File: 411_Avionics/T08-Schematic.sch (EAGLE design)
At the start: 42 parts, among them IC1 BQ24022, J1 USB-MICROB, J3 JST-PH-2-SMT-RA, U1 LP5907, U2 M25P10-AVMN6TP_TR, U3 LSM9DS0, U5 LTC1998, U6 ATMEGA32U4-AU, X1 8MHz

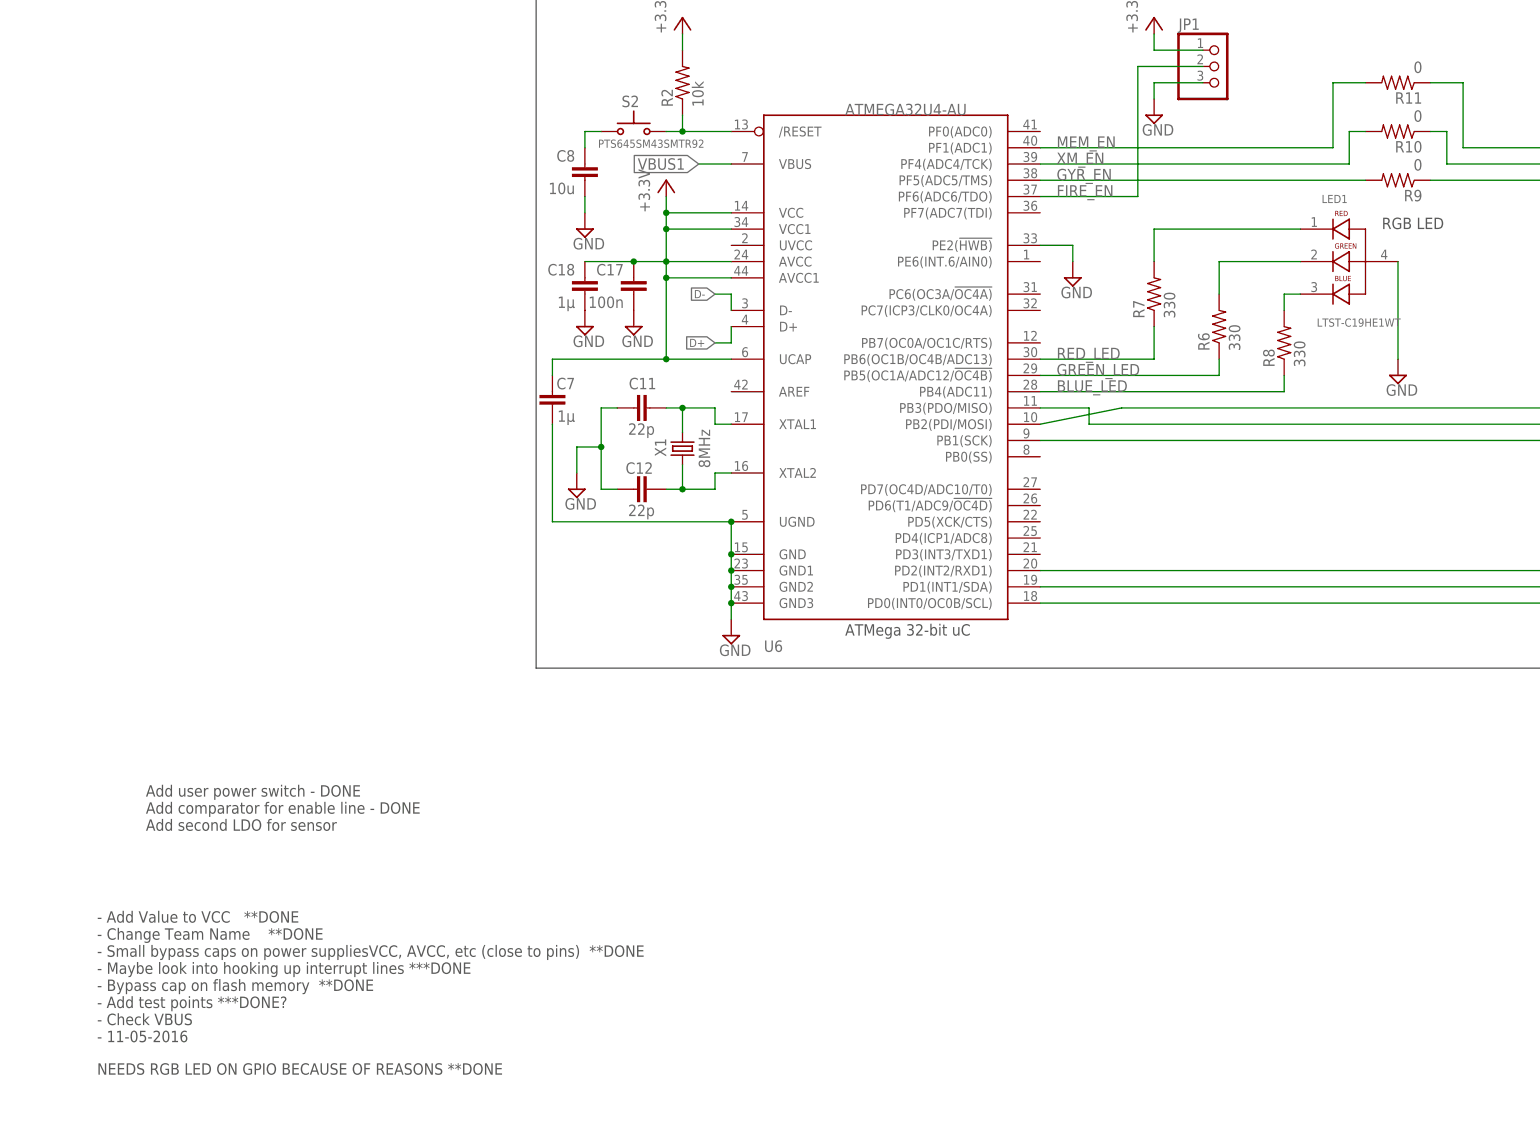
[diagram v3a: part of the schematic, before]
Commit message: Added resistors to D+/D-, removed incorrect reset button cap, fixed RGB LED VCC
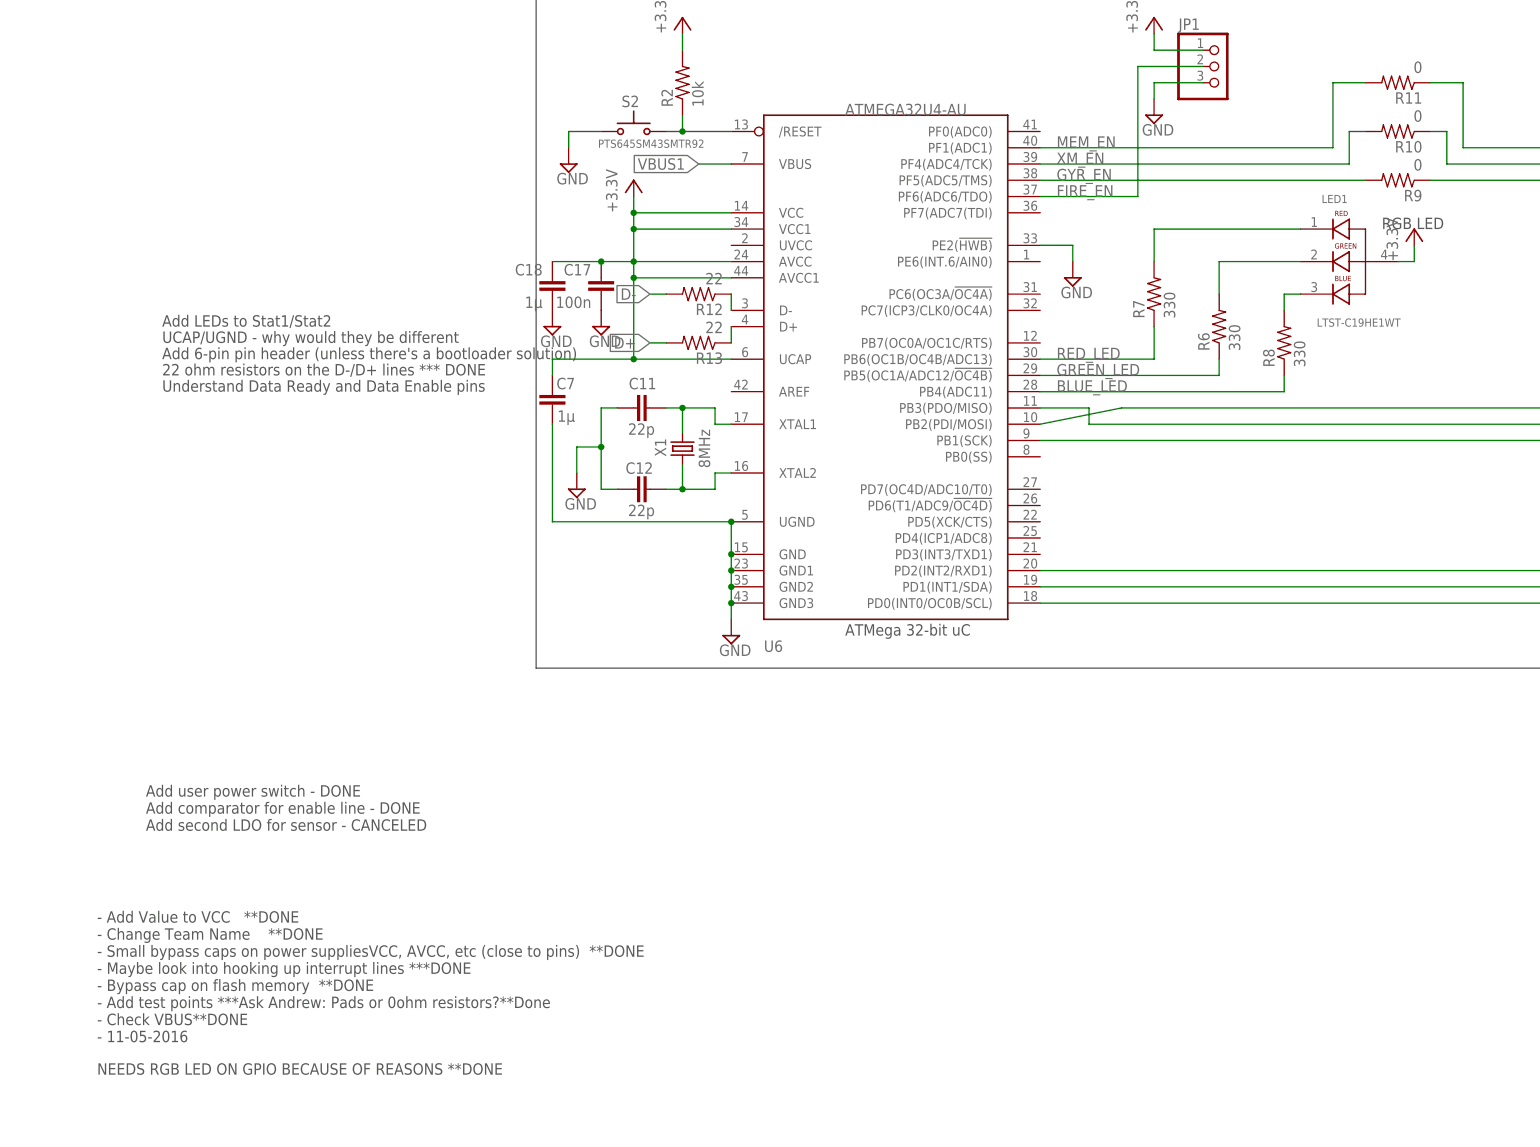
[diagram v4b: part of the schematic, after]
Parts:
- removed C8: 10u, rcl:C-EUC0603
- added R12, R13: 22, rcl:R-US_R0603
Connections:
- new net N$47: R13.1, U6.D+
- net D+: now also R13.2; no longer U6.D+
- net D-: now also R12.2; no longer U6.D-
- net GND: now also S2.P; no longer C8.2, LED1.4
- net N$6: now also R12.1, U6.D-; no longer C8.1, S2.P
- net VCC: now also LED1.4
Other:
- note added: "- Add Value to VCC **DONE - Change Team Name **DONE - Small bypass caps on power suppliesVCC, AVCC, etc (close to pins) **DONE - Maybe look into hooking up interrupt lines ***DONE - Bypass cap on flash memory **DONE - Add test points ***Ask Andrew: Pads or 0ohm resistors?**Done - Check VBUS**DONE - 11-05-2016"
- note added: "22 ohm resistors on the D-/D+ lines *** DONE"
- note added: "Add 6-pin pin header (unless there's a bootloader solution)"
- note added: "Add LEDs to Stat1/Stat2"
- note added: "Add user power switch - DONE Add comparator for enable line - DONE Add second LDO for sensor - CANCELED"
- note added: "UCAP/UGND - why would they be different"
- note added: "Understand Data Ready and Data Enable pins"
- note removed: "- Add Value to VCC **DONE - Change Team Name **DONE - Small bypass caps on power suppliesVCC, AVCC, etc (close to pins) **DONE - Maybe look into hooking up interrupt lines ***DONE - Bypass cap on flash memory **DONE - Add test points ***DONE? - Check VBUS - 11-05-2016"
- note removed: "Add user power switch - DONE Add comparator for enable line - DONE Add second LDO for sensor"
- moved on the sheet: C17, C18

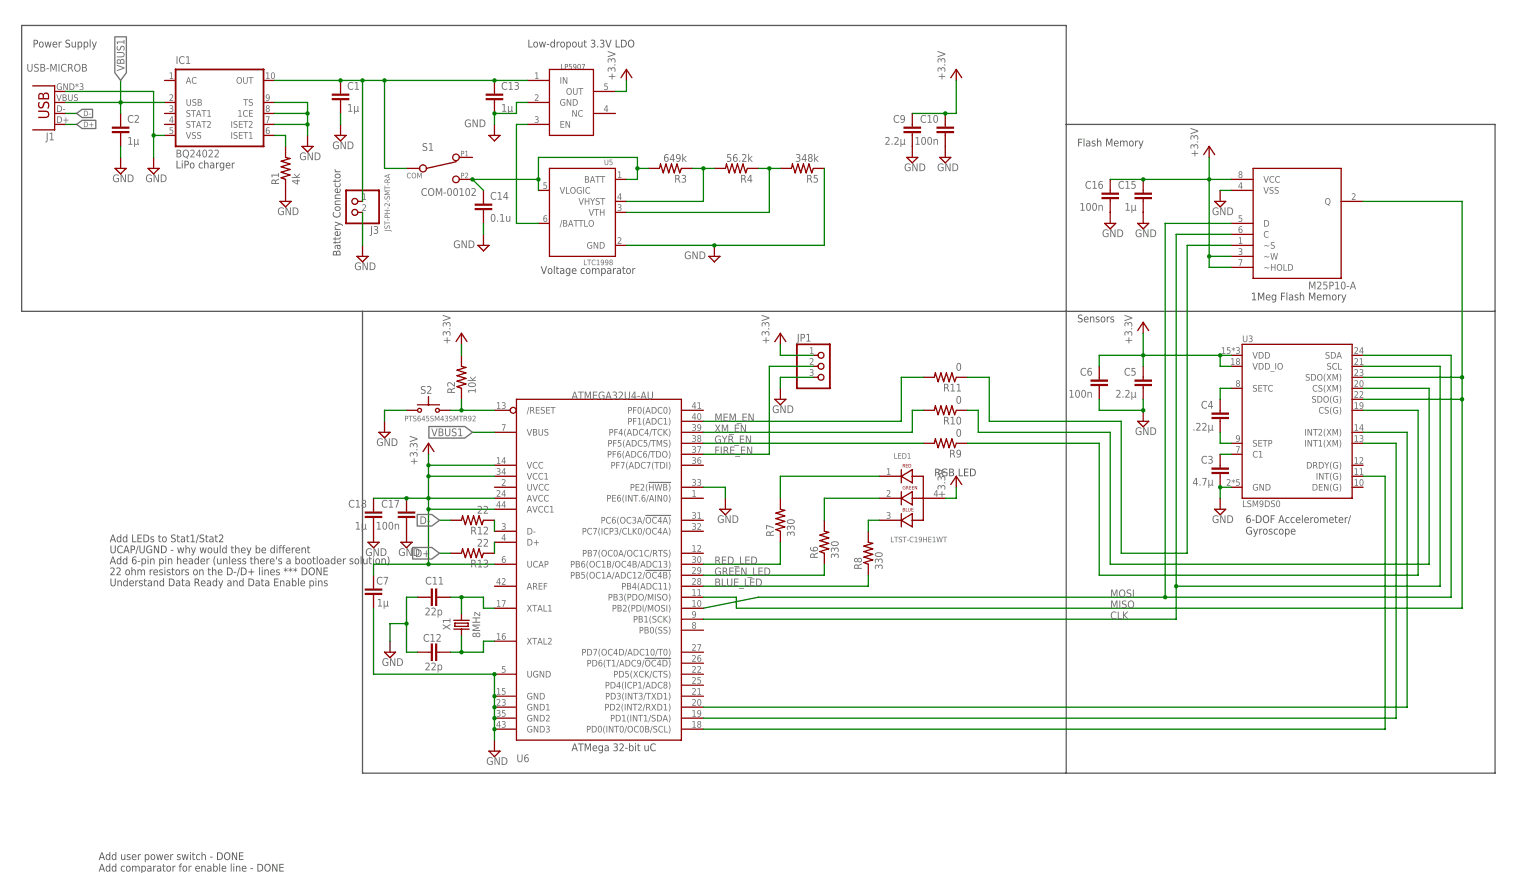
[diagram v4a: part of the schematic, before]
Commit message: Lots of changes to layout!
-Added 6 pin header
-Added status LEDs
-Added Power LEDs`
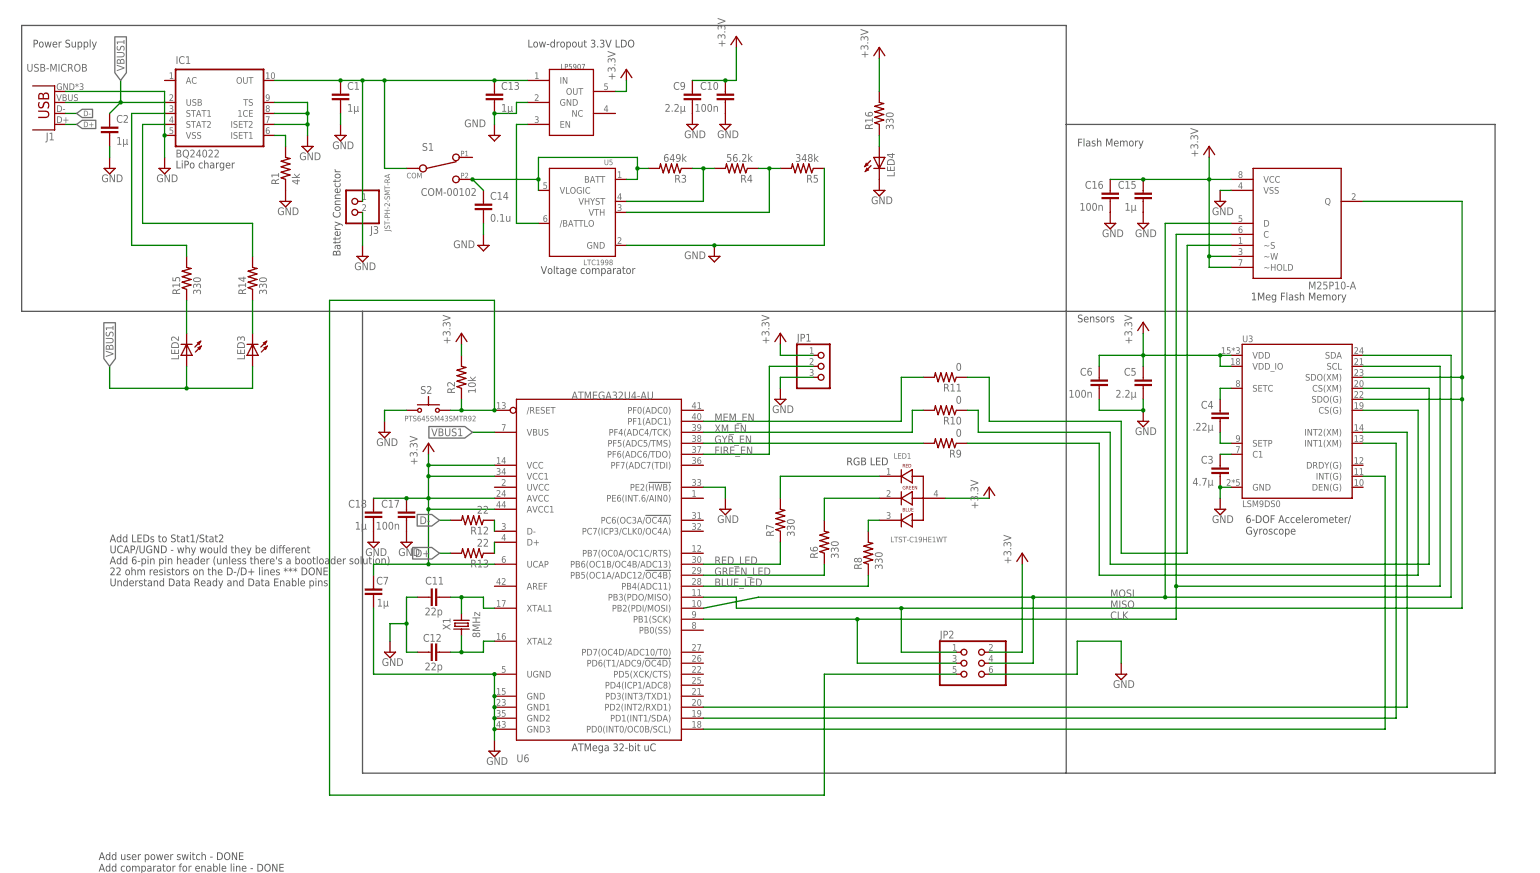
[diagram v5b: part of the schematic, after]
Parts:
- added JP2: (no value), pinhead:PINHD-2X3
- added LED2, LED3, LED4: (no value), adafruit:LEDCHIP-LED0603
- added R14, R15, R16: 330, rcl:R-US_R0805
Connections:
- new net N$48: LED2.C, R15.1
- new net N$49: LED3.C, R14.1
- new net N$50: IC1G$1.STAT1, R15.2
- new net N$51: IC1G$1.STAT2, R14.2
- new net N$53: LED4.A, R16.1
- net CLK: now also JP2.3
- net GND: now also JP2.6, LED4.C
- net MISO: now also JP2.1
- net MOSI: now also JP2.4
- net N$3: now also JP2.5
- net VBUS1: now also LED2.A, LED3.A
- net VCC: now also JP2.2, R16.2
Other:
- moved on the sheet: C10, C2, C9
